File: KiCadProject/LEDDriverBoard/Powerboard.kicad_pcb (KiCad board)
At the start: 4 copper layers, 45 x 45 mm, 30 parts, among them J1 XT30, J2 XT30, J3 JST_SM04B, J4 JST_SM04B, Q1 Q_NMOS_GDS, Q2 SUD50P10-43L-GE3, U1 MAX16833

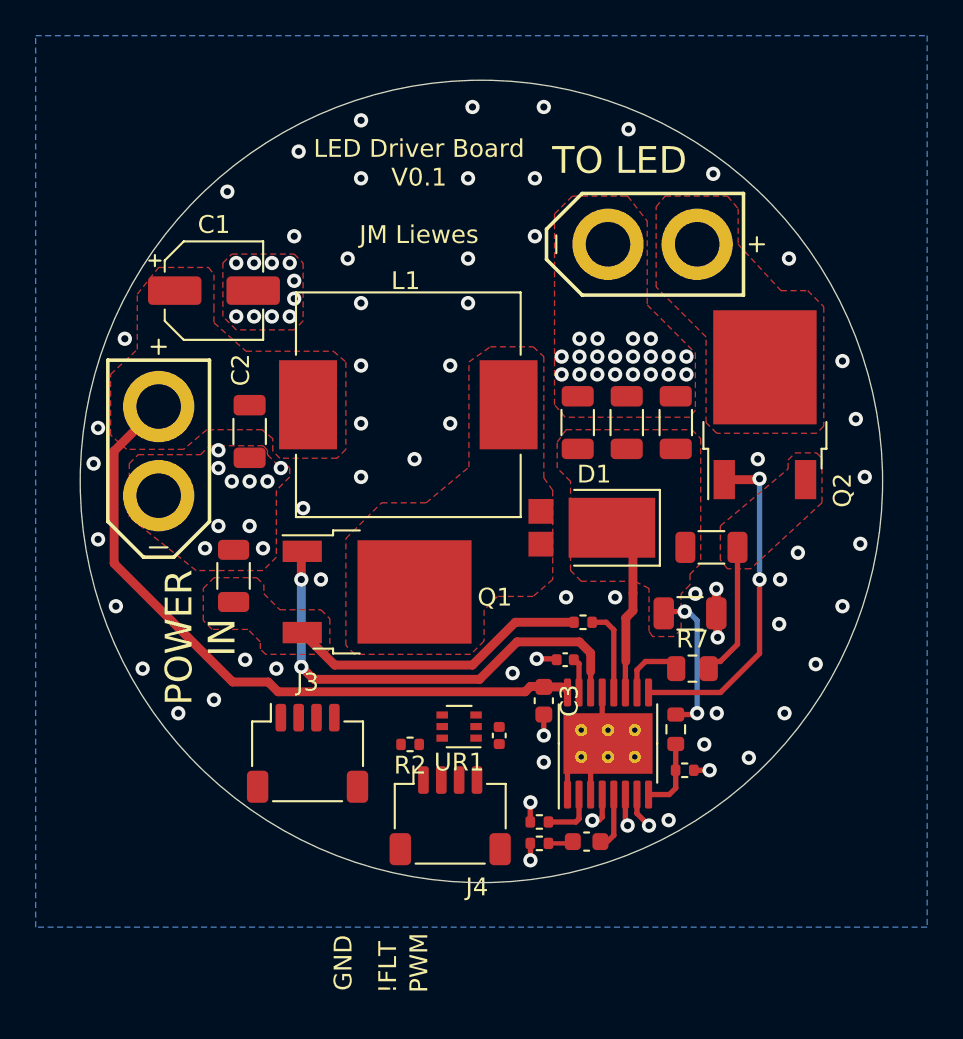
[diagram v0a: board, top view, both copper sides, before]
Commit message: All PCB's should be done. Do a final check before ordering.
Signed-off-by: Eldalote.Electronics <Eldalote.Electronics@gmail.com>
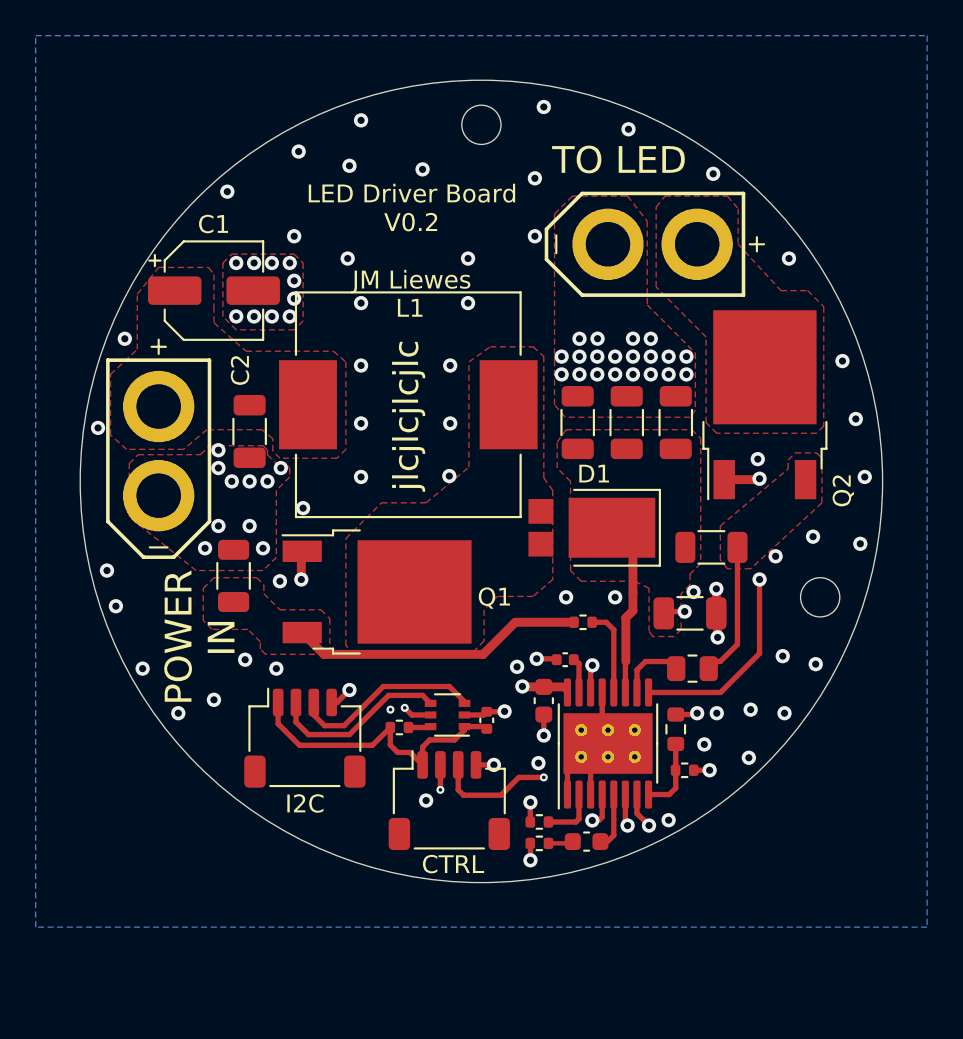
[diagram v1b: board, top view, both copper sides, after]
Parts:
- added REF**: MountingHole_2.2mm_M2, MountingHole:MountingHole_2.2mm_M2, F.Cu at (150.0, 80.0)
- added REF**: MountingHole_2.2mm_M2, MountingHole:MountingHole_2.2mm_M2, F.Cu at (169.0, 106.5)
- moved R2 1.12 mm to (145.4, 113.8)
- moved C10 1.10 mm to (150.3, 113.4)
- moved UR1 0.92 mm to (148.1, 113.1)
- moved J3 0.86 mm to (140.1, 114.4)
- moved J4 0.85 mm to (148.2, 117.9)
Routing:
- net +3V3: track 0.00 -> 16.9 mm
- net /ICTRL: track 2.02 -> 17.6 mm, vias 1 -> 2
- net /!FTL: track 1.79 -> 16.1 mm, vias 1 -> 2
- net /PWMDIM: track 2.02 -> 16.1 mm, vias 1 -> 2
- net /I2C_SCL: track 0.00 -> 10.8 mm
- net /I2C_SDA: track 0.00 -> 10.0 mm
- net /NDRV: track 26.4 -> 21.5 mm
- net GND: track 17.4 -> 21.4 mm, vias 102 -> 105
- net /divider_high: track 0.00 -> 1.26 mm
- net /IN: track 38.5 -> 37.9 mm, vias 0 -> 1
- added copper zone on In3.Cu, net GND
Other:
- copper layers 4 -> 6
- board text added: "CTRL"
- board text added: "I2C"
- board text added: "LED Driver Board V0.2 JM Liewes"
- board text removed: "!FLT"
- board text removed: "GND"
- board text removed: "LED Driver Board V0.1 JM Liewes"
- board text removed: "PWM"

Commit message: Made ready to order PCBs. Some problems with ordering due to misunderstanding. Thinking about solutions
Signed-off-by: Eldalote.Electronics <Eldalote.Electronics@gmail.com>
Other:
- rule pad_to_mask_clearance: 0.05 -> 0
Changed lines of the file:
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@@
       (dielectric_constraints no)
     )
-    (pad_to_mask_clearance 0.05)
-    (solder_mask_min_width 0.254)
+    (pad_to_mask_clearance 0)
     (pcbplotparams
       (layerselection 0x00010fc_ffffffff)
       (disableapertmacros false)
-      (usegerberextensions false)
+      (usegerberextensions true)
       (usegerberattributes true)
       (usegerberadvancedattributes true)
@@
       (plotinvisibletext false)
       (sketchpadsonfab false)
-      (subtractmaskfromsilk false)
+      (subtractmaskfromsilk true)
       (outputformat 1)
       (mirror false)
-      (drillshape 1)
+      (drillshape 0)
       (scaleselection 1)
-      (outputdirectory "")
+      (outputdirectory "Fab/")
     )
   )
@@
     (fp_line (start -1 -0.625) (end 1 -0.625) (layer "F.Fab") (width 0.1))
     (fp_line (start -1 0.625) (end -1 -0.625) (layer "F.Fab") (width 0.1))
-    (pad "1" smd roundrect (at -0.9125 0) (size 1.025 1.4) (layers "F.Cu" "F.Paste" "F.Mask") (roundrect_rratio 0.243902)
+    (pad "1" smd roundrect (at -0.9125 0) (size 1.025 1.4) (layers "F.Cu" "F.Paste" "F.Mask") (roundrect_rratio 0.243902439)
       (net 10 "/ISENSE-") (pintype "passive"))
-    (pad "2" smd roundrect (at 0.9125 0) (size 1.025 1.4) (layers "F.Cu" "F.Paste" "F.Mask") (roundrect_rratio 0.243902)
+    (pad "2" smd roundrect (at 0.9125 0) (size 1.025 1.4) (layers "F.Cu" "F.Paste" "F.Mask") (roundrect_rratio 0.243902439)
       (net 20 "/Vout-FET") (pintype "passive"))
     (model "${KICAD6_3DMODEL_DIR}/Resistor_SMD.3dshapes/R_0805_2012Metric.wrl"
@@
     (pad "4" smd roundrect (at 1.5 -2) (size 0.6 1.55) (layers "F.Cu" "F.Paste" "F.Mask") (roundrect_rratio 0.25)
       (net 1 "GND") (pinfunction "Pin_4") (pintype "passive"))
-    (pad "MP" smd roundrect (at -2.8 1.875) (size 1.2 1.8) (layers "F.Cu" "F.Paste" "F.Mask") (roundrect_rratio 0.208333))
-    (pad "MP" smd roundrect (at 2.8 1.875) (size 1.2 1.8) (layers "F.Cu" "F.Paste" "F.Mask") (roundrect_rratio 0.208333))
+    (pad "MP" smd roundrect (at -2.8 1.875) (size 1.2 1.8) (layers "F.Cu" "F.Paste" "F.Mask") (roundrect_rratio 0.2083333333))
+    (pad "MP" smd roundrect (at 2.8 1.875) (size 1.2 1.8) (layers "F.Cu" "F.Paste" "F.Mask") (roundrect_rratio 0.2083333333))
     (model "F:/Engineering/Projects/Divelamp/KiCadImports/3DModels/SM04B-SRSS-TB.STEP"
       (offset (xyz 0 1.25 -0.5))
@@
     (fp_line (start -1.6 0.8) (end -1.6 -0.8) (layer "F.Fab") (width 0.1))
     (fp_line (start 1.6 -0.8) (end 1.6 0.8) (layer "F.Fab") (width 0.1))
-    (pad "1" smd roundrect (at -1.475 0) (size 1.15 1.8) (layers "F.Cu" "F.Paste" "F.Mask") (roundrect_rratio 0.217391)
+    (pad "1" smd roundrect (at -1.475 0) (size 1.15 1.8) (layers "F.Cu" "F.Paste" "F.Mask") (roundrect_rratio 0.2173913043)
       (net 18 "/V-out") (pintype "passive"))
-    (pad "2" smd roundrect (at 1.475 0) (size 1.15 1.8) (layers "F.Cu" "F.Paste" "F.Mask") (roundrect_rratio 0.217391)
+    (pad "2" smd roundrect (at 1.475 0) (size 1.15 1.8) (layers "F.Cu" "F.Paste" "F.Mask") (roundrect_rratio 0.2173913043)
       (net 1 "GND") (pintype "passive"))
     (model "${KICAD6_3DMODEL_DIR}/Capacitor_SMD.3dshapes/C_1206_3216Metric.wrl"
@@
     (fp_line (start 1.6 -0.8) (end 1.6 0.8) (layer "F.Fab") (width 0.1))
     (fp_line (start -1.6 0.8) (end -1.6 -0.8) (layer "F.Fab") (width 0.1))
-    (pad "1" smd roundrect (at -1.475 0 90) (size 1.15 1.8) (layers "F.Cu" "F.Paste" "F.Mask") (roundrect_rratio 0.217391)
+    (pad "1" smd roundrect (at -1.475 0 90) (size 1.15 1.8) (layers "F.Cu" "F.Paste" "F.Mask") (roundrect_rratio 0.2173913043)
       (net 18 "/V-out") (pintype "passive"))
-    (pad "2" smd roundrect (at 1.475 0 90) (size 1.15 1.8) (layers "F.Cu" "F.Paste" "F.Mask") (roundrect_rratio 0.217391)
+    (pad "2" smd roundrect (at 1.475 0 90) (size 1.15 1.8) (layers "F.Cu" "F.Paste" "F.Mask") (roundrect_rratio 0.2173913043)
       (net 1 "GND") (pintype "passive"))
     (model "${KICAD6_3DMODEL_DIR}/Capacitor_SMD.3dshapes/C_1206_3216Metric.wrl"
@@
     (fp_line (start 1.6 -0.8) (end 1.6 0.8) (layer "F.Fab") (width 0.1))
     (fp_line (start -1.6 0.8) (end -1.6 -0.8) (layer "F.Fab") (width 0.1))
-    (pad "1" smd roundrect (at -1.4625 0 270) (size 1.125 1.75) (layers "F.Cu" "F.Paste" "F.Mask") (roundrect_rratio 0.222222)
-      (net 1 "GND") (pintype "passive"))
-    (pad "2" smd roundrect (at 1.4625 0 270) (size 1.125 1.75) (layers "F.Cu" "F.Paste" "F.Mask") (roundrect_rratio 0.222222)
+    (pad "1" smd roundrect (at -1.4625 0 270) (size 1.125 1.75) (layers "F.Cu" "F.Paste" "F.Mask") (roundrect_rratio 0.2222222222)
+      (net 1 "GND") (pintype "passive"))
+    (pad "2" smd roundrect (at 1.4625 0 270) (size 1.125 1.75) (layers "F.Cu" "F.Paste" "F.Mask") (roundrect_rratio 0.2222222222)
       (net 4 "/RCS") (pintype "passive"))
     (model "${KICAD6_3DMODEL_DIR}/Resistor_SMD.3dshapes/R_1206_3216Metric.wrl"
@@
     (fp_line (start 1.6 -0.8) (end 1.6 0.8) (layer "F.Fab") (width 0.1))
     (fp_line (start -1.6 0.8) (end -1.6 -0.8) (layer "F.Fab") (width 0.1))
-    (pad "1" smd roundrect (at -1.4625 0 180) (size 1.125 1.75) (layers "F.Cu" "F.Paste" "F.Mask") (roundrect_rratio 0.222222)
+    (pad "1" smd roundrect (at -1.4625 0 180) (size 1.125 1.75) (layers "F.Cu" "F.Paste" "F.Mask") (roundrect_rratio 0.2222222222)
       (net 20 "/Vout-FET") (pintype "passive"))
-    (pad "2" smd roundrect (at 1.4625 0 180) (size 1.125 1.75) (layers "F.Cu" "F.Paste" "F.Mask") (roundrect_rratio 0.222222)
+    (pad "2" smd roundrect (at 1.4625 0 180) (size 1.125 1.75) (layers "F.Cu" "F.Paste" "F.Mask") (roundrect_rratio 0.2222222222)
       (net 18 "/V-out") (pintype "passive"))
     (model "${KICAD6_3DMODEL_DIR}/Resistor_SMD.3dshapes/R_1206_3216Metric.wrl"
@@
     (fp_line (start 1.6 0.8) (end -1.6 0.8) (layer "F.Fab") (width 0.1))
     (fp_line (start 1.6 -0.8) (end 1.6 0.8) (layer "F.Fab") (width 0.1))
-    (pad "1" smd roundrect (at -1.475 0 90) (size 1.15 1.8) (layers "F.Cu" "F.Paste" "F.Mask") (roundrect_rratio 0.217391)
+    (pad "1" smd roundrect (at -1.475 0 90) (size 1.15 1.8) (layers "F.Cu" "F.Paste" "F.Mask") (roundrect_rratio 0.2173913043)
       (net 18 "/V-out") (pintype "passive"))
-    (pad "2" smd roundrect (at 1.475 0 90) (size 1.15 1.8) (layers "F.Cu" "F.Paste" "F.Mask") (roundrect_rratio 0.217391)
+    (pad "2" smd roundrect (at 1.475 0 90) (size 1.15 1.8) (layers "F.Cu" "F.Paste" "F.Mask") (roundrect_rratio 0.2173913043)
       (net 1 "GND") (pintype "passive"))
     (model "${KICAD6_3DMODEL_DIR}/Capacitor_SMD.3dshapes/C_1206_3216Metric.wrl"
@@
     (pad "4" smd roundrect (at 1.5 -2) (size 0.6 1.55) (layers "F.Cu" "F.Paste" "F.Mask") (roundrect_rratio 0.25)
       (net 1 "GND") (pinfunction "Pin_4") (pintype "passive"))
-    (pad "MP" smd roundrect (at 2.8 1.875) (size 1.2 1.8) (layers "F.Cu" "F.Paste" "F.Mask") (roundrect_rratio 0.208333))
-    (pad "MP" smd roundrect (at -2.8 1.875) (size 1.2 1.8) (layers "F.Cu" "F.Paste" "F.Mask") (roundrect_rratio 0.208333))
+    (pad "MP" smd roundrect (at 2.8 1.875) (size 1.2 1.8) (layers "F.Cu" "F.Paste" "F.Mask") (roundrect_rratio 0.2083333333))
+    (pad "MP" smd roundrect (at -2.8 1.875) (size 1.2 1.8) (layers "F.Cu" "F.Paste" "F.Mask") (roundrect_rratio 0.2083333333))
     (model "F:/Engineering/Projects/Divelamp/KiCadImports/3DModels/SM04B-SRSS-TB.STEP"
       (offset (xyz 0 1.25 -0.5))
@@
     (fp_line (start -1.6 -0.8) (end 1.6 -0.8) (layer "F.Fab") (width 0.1))
     (fp_line (start 1.6 0.8) (end -1.6 0.8) (layer "F.Fab") (width 0.1))
-    (pad "1" smd roundrect (at -1.475 0 270) (size 1.15 1.8) (layers "F.Cu" "F.Paste" "F.Mask") (roundrect_rratio 0.217391)
+    (pad "1" smd roundrect (at -1.475 0 270) (size 1.15 1.8) (layers "F.Cu" "F.Paste" "F.Mask") (roundrect_rratio 0.2173913043)
       (net 14 "/IN") (pintype "passive"))
-    (pad "2" smd roundrect (at 1.475 0 270) (size 1.15 1.8) (layers "F.Cu" "F.Paste" "F.Mask") (roundrect_rratio 0.217391)
+    (pad "2" smd roundrect (at 1.475 0 270) (size 1.15 1.8) (layers "F.Cu" "F.Paste" "F.Mask") (roundrect_rratio 0.2173913043)
       (net 1 "GND") (pintype "passive"))
     (model "${KICAD6_3DMODEL_DIR}/Capacitor_SMD.3dshapes/C_1206_3216Metric.wrl"
@@
     (fp_line (start 1.6 -0.8) (end 1.6 0.8) (layer "F.Fab") (width 0.1))
     (fp_line (start 1.6 0.8) (end -1.6 0.8) (layer "F.Fab") (width 0.1))
-    (pad "1" smd roundrect (at -1.475 0 90) (size 1.15 1.8) (layers "F.Cu" "F.Paste" "F.Mask") (roundrect_rratio 0.217391)
+    (pad "1" smd roundrect (at -1.475 0 90) (size 1.15 1.8) (layers "F.Cu" "F.Paste" "F.Mask") (roundrect_rratio 0.2173913043)
       (net 18 "/V-out") (pintype "passive"))
-    (pad "2" smd roundrect (at 1.475 0 90) (size 1.15 1.8) (layers "F.Cu" "F.Paste" "F.Mask") (roundrect_rratio 0.217391)
+    (pad "2" smd roundrect (at 1.475 0 90) (size 1.15 1.8) (layers "F.Cu" "F.Paste" "F.Mask") (roundrect_rratio 0.2173913043)
       (net 1 "GND") (pintype "passive"))
     (model "${KICAD6_3DMODEL_DIR}/Capacitor_SMD.3dshapes/C_1206_3216Metric.wrl"

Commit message: Started work on body 3d work
Signed-off-by: Eldalote.Electronics <Eldalote.Electronics@gmail.com>
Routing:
- net /IN: track 37.9 -> 37.3 mm
- net GND: vias 105 -> 107
- removed copper zone on In3.Cu, net GND
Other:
- copper layers 6 -> 4
